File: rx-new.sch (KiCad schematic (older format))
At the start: 96 parts, among them J1 RF_IN, J2 PWR_IN, J3 IQ_OUT, J4 4LO_IN, Q1 BC848, Q2 BC858, Q3 BC848, Q4 BC858, U1 TPS79101DBVREP, U2 SN74CBT3253, U3 AD797, U4 AD797, U5 NC7SZ00M5X, U6 OPA1662, U7 74AUP1G74, U8 74AUP1G74

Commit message: Added mounting holes and small layout changes
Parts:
- added H1, H2, H3, H4: MountingHole_Pad, MountingHole:MountingHole_3.2mm_M3_DIN965_Pad, symbol Mechanical:MountingHole_Pad
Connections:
- net GND: now also H1.1, H2.1, H3.1, H4.1
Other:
- note added: "Mounting holes"
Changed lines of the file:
@@
 Wire Wire Line
 	2600 6650 3000 6650
+$Comp
+L Mechanical:MountingHole_Pad H1
+U 1 1 5F7AA574
+P 6350 6850
+F 0 "H1" H 6450 6853 50  0000 L CNN
+F 1 "MountingHole_Pad" H 6450 6808 50  0001 L CNN
+F 2 "MountingHole:MountingHole_3.2mm_M3_DIN965_Pad" H 6350 6850 50  0001 C CNN
+F 3 "~" H 6350 6850 50  0001 C CNN
+	1    6350 6850
+	1    0    0    -1
+$EndComp
+$Comp
+L power:GND #PWR011
+U 1 1 5F7AC58A
+P 6350 6950
+F 0 "#PWR011" H 6350 6700 50  0001 C CNN
+F 1 "GND" H 6355 6777 50  0001 C CNN
+F 2 "" H 6350 6950 50  0001 C CNN
+F 3 "" H 6350 6950 50  0001 C CNN
+	1    6350 6950
+	1    0    0    -1
+$EndComp
+$Comp
+L Mechanical:MountingHole_Pad H2
+U 1 1 5F7ACD2E
+P 6350 7200
+F 0 "H2" H 6450 7203 50  0000 L CNN
+F 1 "MountingHole_Pad" H 6450 7158 50  0001 L CNN
+F 2 "MountingHole:MountingHole_3.2mm_M3_DIN965_Pad" H 6350 7200 50  0001 C CNN
+F 3 "~" H 6350 7200 50  0001 C CNN
+	1    6350 7200
+	1    0    0    -1
+$EndComp
+$Comp
+L power:GND #PWR034
+U 1 1 5F7ACD34
+P 6350 7300
+F 0 "#PWR034" H 6350 7050 50  0001 C CNN
+F 1 "GND" H 6355 7127 50  0001 C CNN
+F 2 "" H 6350 7300 50  0001 C CNN
+F 3 "" H 6350 7300 50  0001 C CNN
+	1    6350 7300
+	1    0    0    -1
+$EndComp
+$Comp
+L power:GND #PWR038
+U 1 1 5F7C090E
+P 6650 6950
+F 0 "#PWR038" H 6650 6700 50  0001 C CNN
+F 1 "GND" H 6655 6777 50  0001 C CNN
+F 2 "" H 6650 6950 50  0001 C CNN
+F 3 "" H 6650 6950 50  0001 C CNN
+	1    6650 6950
+	1    0    0    -1
+$EndComp
+$Comp
+L Mechanical:MountingHole_Pad H4
+U 1 1 5F7D421A
+P 6650 7200
+F 0 "H4" H 6750 7203 50  0000 L CNN
+F 1 "MountingHole_Pad" H 6750 7158 50  0001 L CNN
+F 2 "MountingHole:MountingHole_3.2mm_M3_DIN965_Pad" H 6650 7200 50  0001 C CNN
+F 3 "~" H 6650 7200 50  0001 C CNN
+	1    6650 7200
+	1    0    0    -1
+$EndComp
+$Comp
+L power:GND #PWR045
+U 1 1 5F7D4220
+P 6650 7300
+F 0 "#PWR045" H 6650 7050 50  0001 C CNN
+F 1 "GND" H 6655 7127 50  0001 C CNN
+F 2 "" H 6650 7300 50  0001 C CNN
+F 3 "" H 6650 7300 50  0001 C CNN
+	1    6650 7300
+	1    0    0    -1
+$EndComp
+Text Notes 6250 6650 0    50   ~ 0
+Mounting holes
+$Comp
+L Mechanical:MountingHole_Pad H3
+U 1 1 5F7C0908
+P 6650 6850
+F 0 "H3" H 6750 6853 50  0000 L CNN
+F 1 "MountingHole_Pad" H 6750 6808 50  0001 L CNN
+F 2 "MountingHole:MountingHole_3.2mm_M3_DIN965_Pad" H 6650 6850 50  0001 C CNN
+F 3 "~" H 6650 6850 50  0001 C CNN
+	1    6650 6850
+	1    0    0    -1
+$EndComp
 $EndSCHEMATC

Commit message: changed_R_values
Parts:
- R12, R13: value 1E -> 10k?
- R23, R24: value 1E -> 100E
- R3: value 100k -> 56k
- R4: value 100k -> 6k8
- R7: value 1E -> 22E
- R8: value 100k -> 120k
- R9: value 100k -> 27k
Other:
- note added: "+Vf = 6.67V unless R9 = 33k//180k"
- note added: "R12/13 define system gain"
- note added: "play with R4/R3 until -Vf approx 1.5v"
- note removed: "Still need to define all resistor values to generate +Vf and -Vf"
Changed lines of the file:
@@
 P 3150 5600
 F 0 "R8" V 2945 5600 50  0000 C CNN
-F 1 "100k" V 3036 5600 50  0000 C CNN
+F 1 "120k" V 3036 5600 50  0000 C CNN
 F 2 "Resistor_SMD:R_0805_2012Metric_Pad1.15x1.40mm_HandSolder" H 3150 5600 50  0001 C CNN
 F 3 "~" H 3150 5600 50  0001 C CNN
@@
 P 3150 5800
 F 0 "R9" V 2945 5800 50  0000 C CNN
-F 1 "100k" V 3036 5800 50  0000 C CNN
+F 1 "27k" V 3036 5800 50  0000 C CNN
 F 2 "Resistor_SMD:R_0805_2012Metric_Pad1.15x1.40mm_HandSolder" H 3150 5800 50  0001 C CNN
 F 3 "~" H 3150 5800 50  0001 C CNN
@@
 P 2100 6650
 F 0 "R7" V 1895 6650 50  0000 C CNN
-F 1 "1E" V 1986 6650 50  0000 C CNN
+F 1 "22E" V 1986 6650 50  0000 C CNN
 F 2 "Resistor_SMD:R_0805_2012Metric_Pad1.15x1.40mm_HandSolder" H 2100 6650 50  0001 C CNN
 F 3 "~" H 2100 6650 50  0001 C CNN
@@
 Text Notes 2450 6550 0    50   ~ 0
 -Vf = 1.5V
-Text Notes 800  7700 0    50   ~ 0
-Still need to define all resistor values to generate +Vf and -Vf
 Text Notes 3700 7700 0    50   ~ 0
 Every supply C should be a tripple, high value (47µF, mid 0.1µf, small 1nF)
@@
 P 7350 2200
 F 0 "R12" V 7300 2050 50  0000 C CNN
-F 1 "1E" V 7300 2350 50  0000 C CNN
+F 1 "10k?" V 7300 2350 50  0000 C CNN
 F 2 "Resistor_SMD:R_0805_2012Metric_Pad1.15x1.40mm_HandSolder" H 7350 2200 50  0001 C CNN
 F 3 "~" H 7350 2200 50  0001 C CNN
@@
 P 7350 3900
 F 0 "R13" V 7250 3750 50  0000 C CNN
-F 1 "1E" V 7250 4000 50  0000 C CNN
+F 1 "10k?" V 7250 4000 50  0000 C CNN
 F 2 "Resistor_SMD:R_0805_2012Metric_Pad1.15x1.40mm_HandSolder" H 7350 3900 50  0001 C CNN
 F 3 "~" H 7350 3900 50  0001 C CNN
@@
 P 8950 1650
 F 0 "R23" V 8745 1650 50  0000 C CNN
-F 1 "1E" V 8836 1650 50  0000 C CNN
+F 1 "100E" V 8836 1650 50  0000 C CNN
 F 2 "Resistor_SMD:R_0805_2012Metric_Pad1.15x1.40mm_HandSolder" H 8950 1650 50  0001 C CNN
 F 3 "~" H 8950 1650 50  0001 C CNN
@@
 P 8950 3350
 F 0 "R24" V 8745 3350 50  0000 C CNN
-F 1 "1E" V 8836 3350 50  0000 C CNN
+F 1 "100E" V 8836 3350 50  0000 C CNN
 F 2 "Resistor_SMD:R_0805_2012Metric_Pad1.15x1.40mm_HandSolder" H 8950 3350 50  0001 C CNN
 F 3 "~" H 8950 3350 50  0001 C CNN
@@
 P 1250 7150
 F 0 "R4" V 1045 7150 50  0000 C CNN
-F 1 "100k" V 1136 7150 50  0000 C CNN
+F 1 "6k8" V 1136 7150 50  0000 C CNN
 F 2 "Resistor_SMD:R_0805_2012Metric_Pad1.15x1.40mm_HandSolder" H 1250 7150 50  0001 C CNN
 F 3 "~" H 1250 7150 50  0001 C CNN
@@
 P 1250 6650
 F 0 "R3" V 1045 6650 50  0000 C CNN
-F 1 "100k" V 1136 6650 50  0000 C CNN
+F 1 "56k" V 1136 6650 50  0000 C CNN
 F 2 "Resistor_SMD:R_0805_2012Metric_Pad1.15x1.40mm_HandSolder" H 1250 6650 50  0001 C CNN
 F 3 "~" H 1250 6650 50  0001 C CNN
@@
 	1    0    0    -1
 $EndComp
+Text Notes 2700 5250 0    50   ~ 0
++Vf = 6.67V unless R9 = 33k//180k
+Text Notes 7050 2550 0    50   ~ 0
+R12/13 define system gain
+Text Notes 800  7500 0    50   ~ 0
+play with R4/R3 until -Vf approx 1.5v
 $EndSCHEMATC

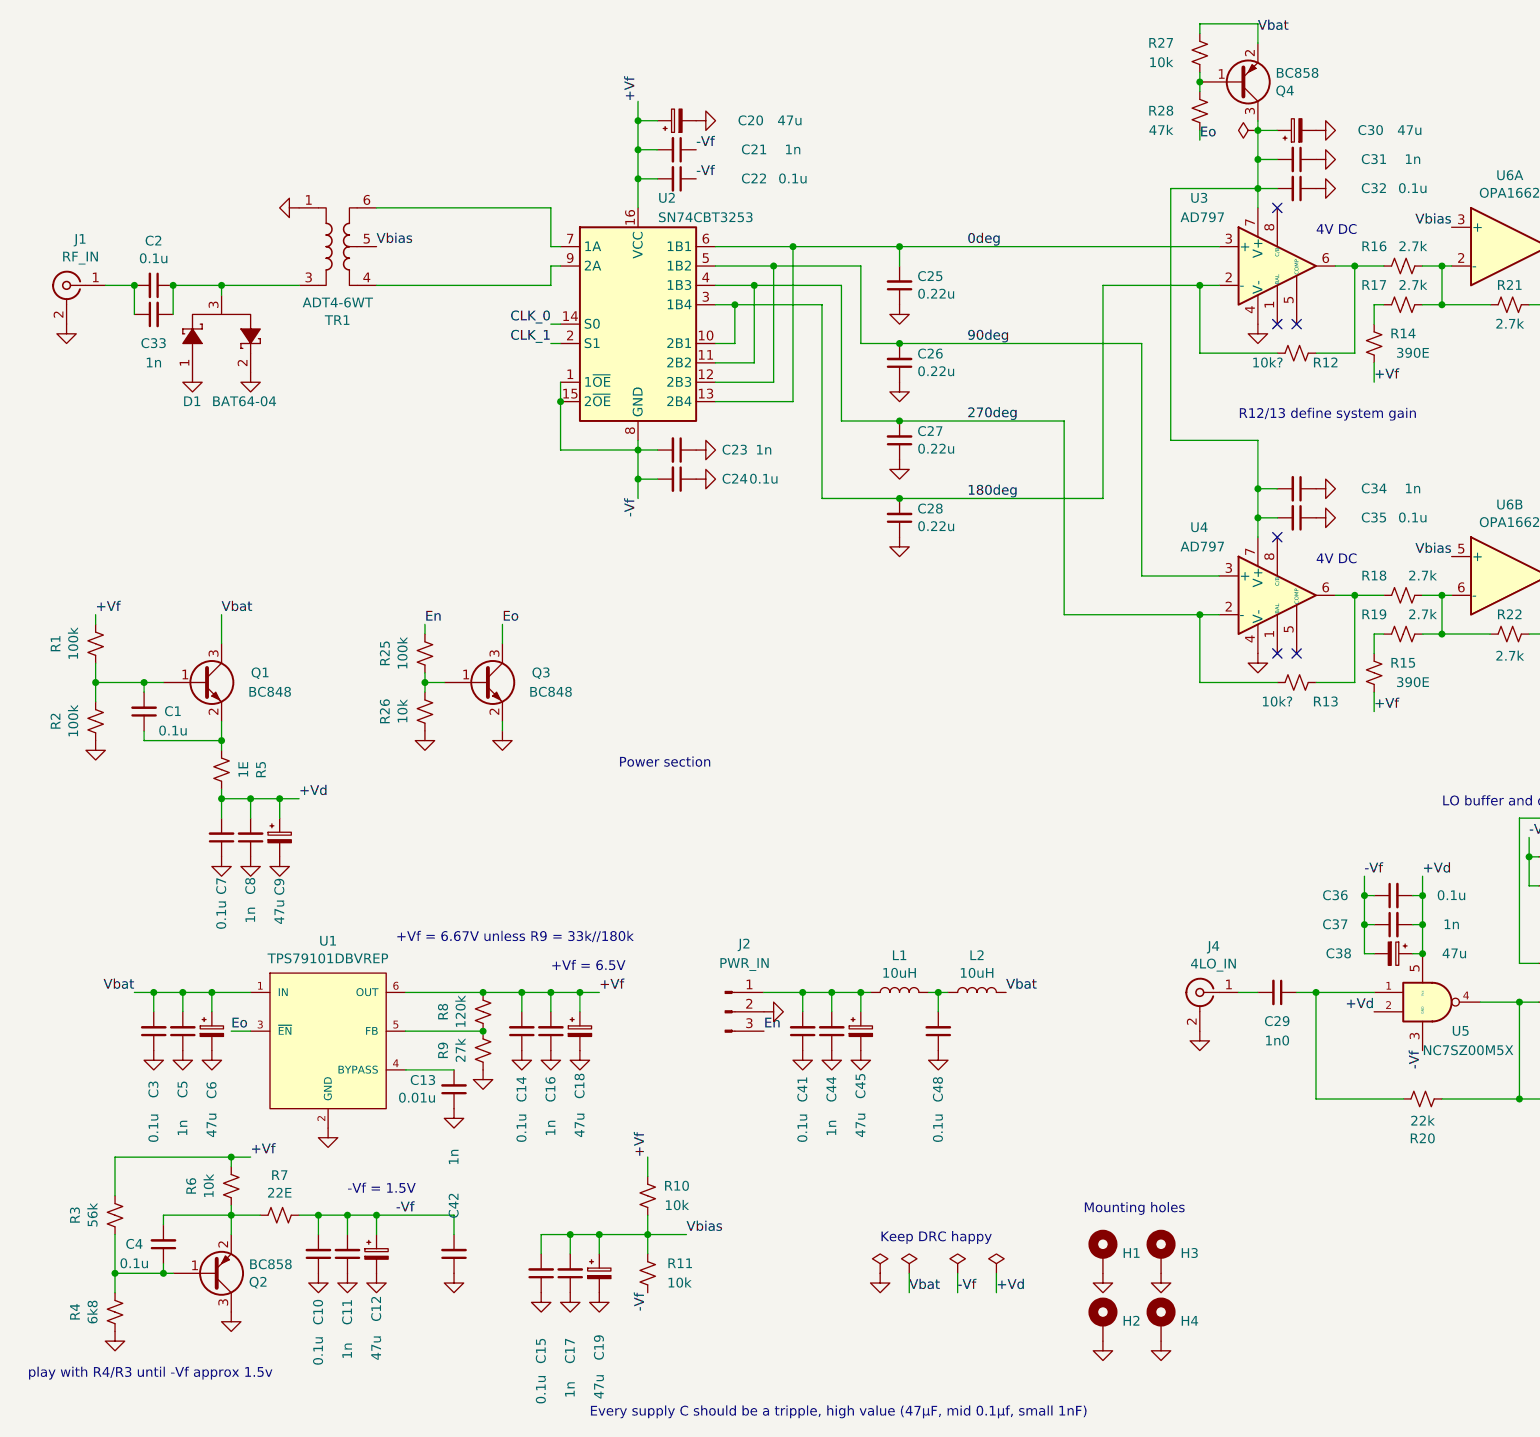
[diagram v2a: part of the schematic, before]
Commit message: Updated voltages and updated opamp feedbacks + reworked En section
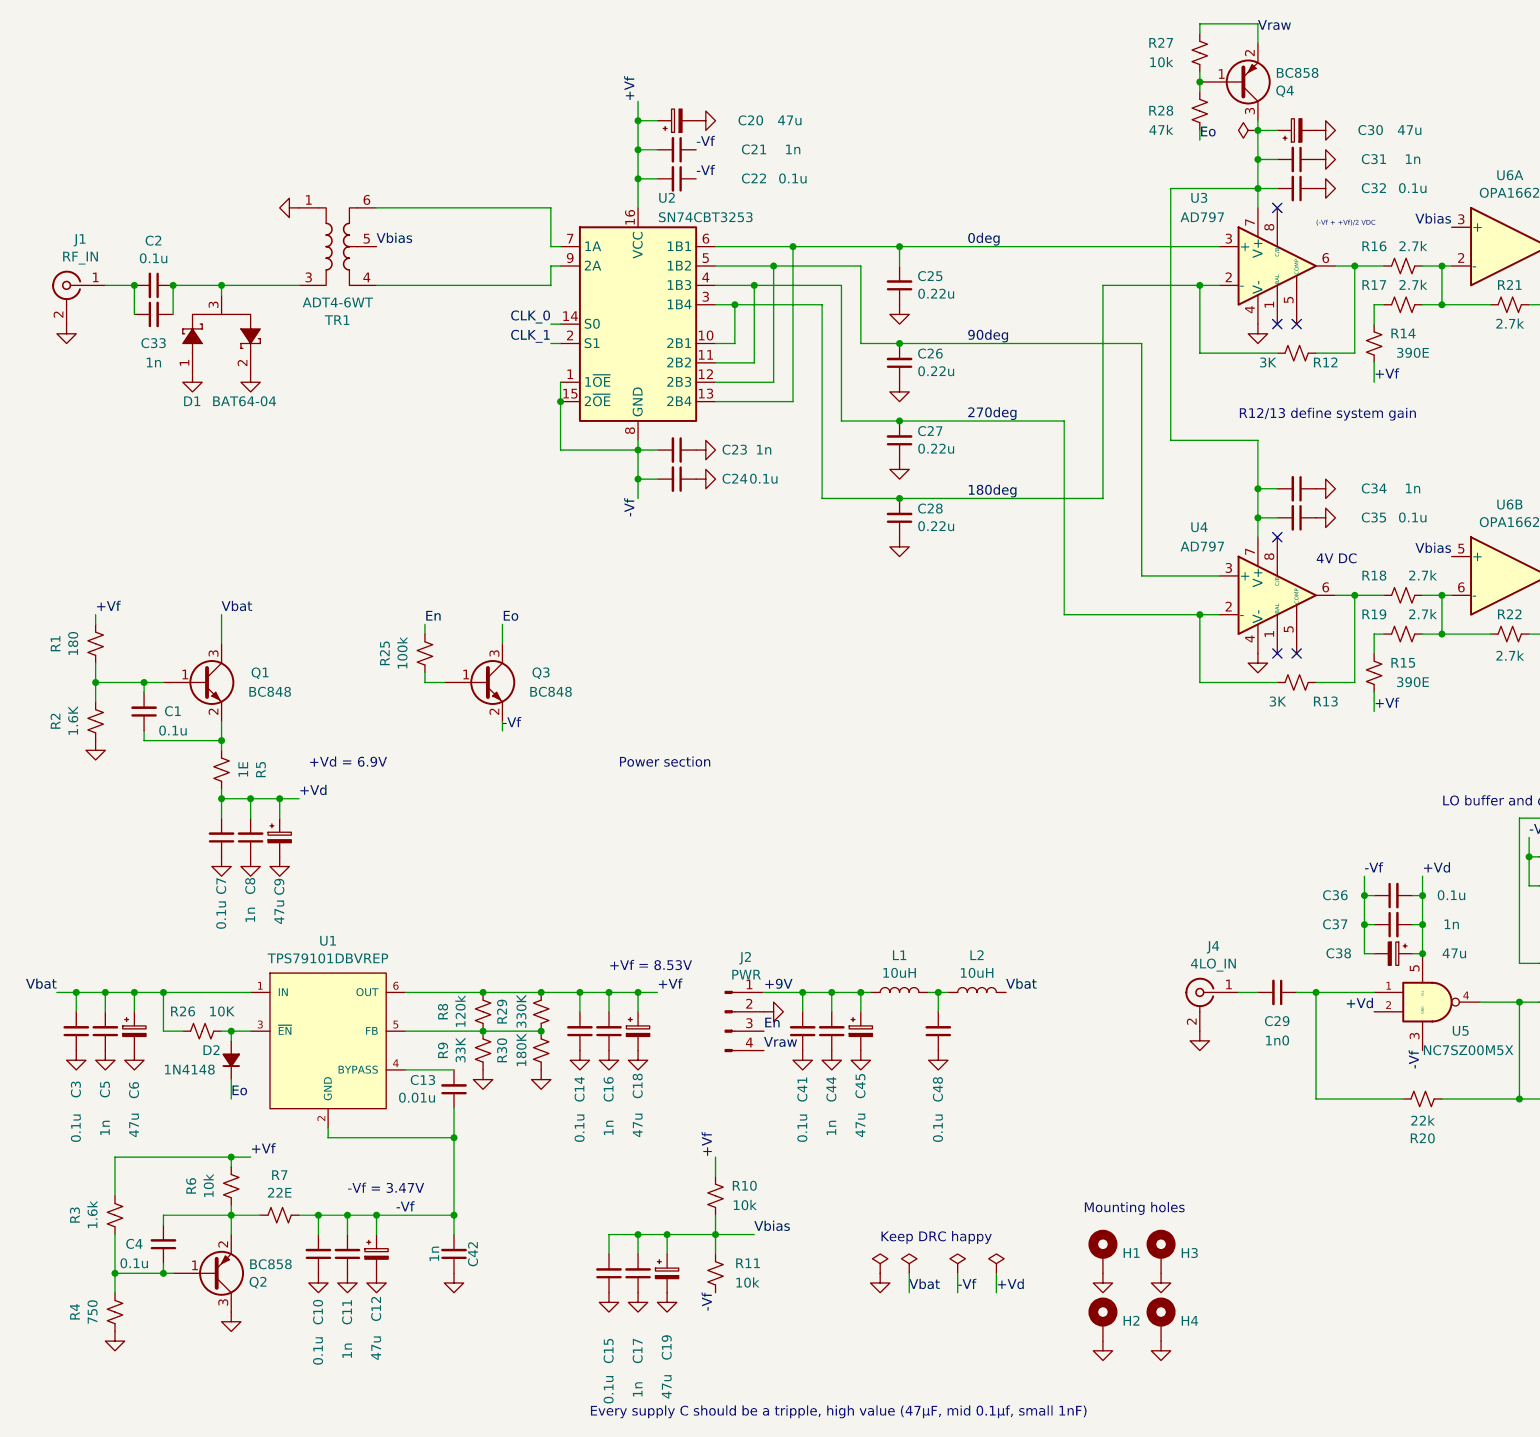
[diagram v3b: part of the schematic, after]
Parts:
- removed J2: PWR_IN, Connector_PinHeader_2.54mm:PinHeader_1x03_P2.54mm_Vertical, symbol Connector:Conn_01x03_Male
- added D2: 1N4148, symbol Device:D_Small_ALT
- added J2: PWR, symbol Connector:Conn_01x04_Male
- added R29: 330K, Resistor_SMD:R_0805_2012Metric_Pad1.15x1.40mm_HandSolder, symbol Device:R_Small_US
- added R30: 180K, Resistor_SMD:R_0805_2012Metric_Pad1.15x1.40mm_HandSolder, symbol Device:R_Small_US
- R1: value 100k -> 180
- R12, R13: value 10k? -> 3K
- R2: value 100k -> 1.6K
- R26: value 10k -> 10K
- R3: value 56k -> 1.6k
- R4: value 6k8 -> 750
- R9: value 27k -> 33K
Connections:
- net +Vf: now also R29.1
- net -Vf: now also C13.1, Q3.2 (E), U1.2 (GND)
- net En: now also J2.3 (Pin_3)
- net Eo: now also D2.1 (K); no longer U1.3 (~EN~)
- net GND: now also J2.2 (Pin_2), R30.1; no longer C13.1, Q3.2 (E), R26.2, U1.2 (GND)
- net Vbat: now also R26.2; no longer Q4.2 (E), R27.2
- net at R8.2, R9.1, U1.5 (FB): now also R29.2, R30.2
- net +9V: now reaches C41.2, C44.2, C45.1, L1.1
- net +9V: now also J2.1 (Pin_1)
- net at Q3.1 (B), R25.2: no longer R26.1
- new net: D2.2 (A), R26.1, U1.3 (~EN~)
- new net Vraw: J2.4 (Pin_4), Q4.2 (E), R27.2
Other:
- note added: "(-Vf + +Vf)/2 VDC"
- note added: "+Vd = 6.9V"
- note added: "+Vf = 8.53V"
- note added: "-Vf = 3.47V"
- note removed: "+Vf = 6.5V"
- note removed: "+Vf = 6.67V unless R9 = 33k//180k"
- note removed: "-Vf = 1.5V"
- note removed: "play with R4/R3 until -Vf approx 1.5v"
- moved on the sheet: C14, C15, C16, C17, C18, C19, C3, C5, C6, R10, R11
